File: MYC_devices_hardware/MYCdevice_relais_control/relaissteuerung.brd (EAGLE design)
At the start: 106.7 x 72.1 mm, 54 parts, among them IC1 MEGA8-P, IC2 7805T, K1 RT424012, K2 RT424012, K3 RT424012, K4 RT424012, Q1 20MHz, T1 BC547, T2 BC547, T3 BC547, T4 BC547

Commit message: adation to "0" based, and minor changes
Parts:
- removed C8: 18pF, resistor:C050-025X075
- removed C9: 100nF, resistor:C050-025X075
- removed R10: 3.3k, eagle-ltspice:0204/7
- added JP2: ISP, jumper:JP3Q
- added R12: 3.3k, rcl:0204V
- added X4, X5: 1503_09, con-lumberg:1503_09
- C1: value 100nF -> 22u 1206; device resistor:C050-025X075 -> resistor:C1206
- C2, C3: value 47uF -> 22u 1206; device rcl:TT5D10 -> resistor:C1206
- C4: value 100nF -> 18pF
- C6: device resistor:C050-025X075 -> resistor:C1206
- D1, D2, D3, D4, D5: device diode:DO41-10 -> zetex:E2LINE
- IC2: value 7805T -> 7805TV; device linear:TO220H -> linear:TO220V
- R1, R2, R4, R6: device rcl:0204/7 -> rcl:0204V
- R8: device eagle-ltspice:0204/7 -> rcl:0204V
- moved C3 57.1 mm to (87.6, 62.2), flipped to the bottom, turned to 0 degrees
- moved IC2 54.6 mm to (72.4, 43.2), turned to 0 degrees
- moved C4 52.4 mm to (97.8, 49.5), turned to 0 degrees
- moved R4 40.7 mm to (25.4, 36.8)
- moved R2 21.6 mm to (74.9, 53.3)
- moved R8 20.3 mm to (53.3, 38.1), turned to 270 degrees
- moved C2 19.9 mm to (76.2, 36.8), flipped to the bottom, turned to 0 degrees
- moved D5 18.0 mm to (73.7, 45.7), turned to 270 degrees
- moved R1 15.3 mm to (74.9, 49.5)
- moved C6 13.7 mm to (95.2, 62.2), flipped to the bottom
- moved SL1 11.7 mm to (85.1, 52.1), turned to 180 degrees
- moved C7 9.67 mm to (108.0, 52.1), turned to 90 degrees
- moved C1 9.25 mm to (69.8, 36.8), flipped to the bottom, turned to 180 degrees
- moved R6 8.98 mm to (40.6, 36.8), turned to 180 degrees
- moved JP1 8.13 mm to (108.0, 44.5)
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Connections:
- net N$37 renamed C5
- removed net N$1: IC1.27, R2.2, SL1.5
- new net N$37: IC1.27, R2.2, SL1.5, X4.3, X5.3
- new net N$56: C16.2, IC1.19, JP2.3, X1.A5
- net GND: now also C2.2, C3.1, C4.1, JP2.6, X4.1, X5.1; no longer C2.-, C3.-, C4.2, C8.1, C9.1
- net N$13: now also R8.2; no longer R6.1
- net N$15: now also R12.1; no longer R4.1
- net N$19: now also C4.2; no longer C8.2
- net N$22: now also R8.1; no longer R6.2
- net N$23: now also JP2.4
- net N$25: now also D5.2; no longer D5.A
- net N$26: now also R6.1; no longer R8.1
- net N$3: now also D1.1, D2.1, D3.1, D4.1, D5.1; no longer C2.+, D1.C, D2.C, D3.C, D4.C, D5.C
- net N$33: now also JP2.1
- net N$34: now also R6.2; no longer R8.2
- net N$35: now also C3.2; no longer C9.2
- net N$36: now also R12.2; no longer R4.2
- net N$40: now also D3.2; no longer D3.A
- net N$41: now also D2.2; no longer D2.A
- net N$42: now also D1.2; no longer D1.A
- net N$5: now also X4.2, X5.2
- net N$66: now also D4.2; no longer D4.A
- net N$67: now also R4.2; no longer R10.2
- net N$69: now also R4.1; no longer R10.1
- net N$7: now also IC1.1, JP2.5; no longer C16.2, IC1.19, X1.A5
- net VDD: now also C2.1, JP2.2; no longer C3.+, C4.1
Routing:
- net N$3: track 193.9 -> 108.2 mm
- net N$56: track 0.00 -> 46.2 mm
- net N$1: track 45.7 -> 0.00 mm
- net N$37: track 0.00 -> 39.6 mm
- net VDD: track 101.2 -> 77.8 mm
- net GND: track 238.4 -> 216.1 mm
- net N$7: track 35.5 -> 13.8 mm
- net N$69: track 91.4 -> 71.2 mm
- net N$26: track 69.8 -> 52.9 mm
- net N$5: track 40.6 -> 55.0 mm
- net N$55: track 48.2 -> 34.6 mm
- net N$23: track 35.5 -> 48.7 mm
- net N$33: track 35.5 -> 48.6 mm
- net N$22: track 48.3 -> 37.4 mm
- net N$62: track 45.7 -> 34.8 mm
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- added copper zone on layer 1, net GND
- added copper zone on layer 16, net GND
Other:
- board size 106.7 x 72.1 mm -> 106.7 x 59.7 mm
- board text added: "Relaissteuerung V02.0"
- board text removed: "Relaisteuerung V01.3"

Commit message: Modified Answer format
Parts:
- removed IC2: 7805TV, linear:TO220V
- added IC3: 78L05, v-reg:78LXX
- added JP3: Power, jumper:JP1
- R1, R2: device rcl:0204V -> resistor:R1206
- X1: value (none) -> Inputs
- X2: value (none) -> Relais1
- X3: value (none) -> Relais2
- moved R1 22.9 mm to (94.0, 36.8), flipped to the bottom, turned to 180 degrees
- moved R2 14.4 mm to (85.1, 43.2), flipped to the bottom, turned to 90 degrees
- moved D5 2.54 mm to (71.1, 45.7)
- moved C4 1.27 mm to (99.1, 49.5), turned to 180 degrees
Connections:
- new net N$58: C6.1, IC1.20, IC1.7, JP2.2, JP3.2
- net GND: now also IC3.GND; no longer IC2.2
- net N$3: now also IC3.IN; no longer IC2.1
- net VDD: now also IC3.OUT, JP3.1; no longer C6.1, IC1.20, IC1.7, IC2.3, JP2.2
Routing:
- net N$58: track 0.00 -> 70.6 mm
- net VDD: track 77.8 -> 30.1 mm
- net N$37: track 39.6 -> 53.0 mm
- net N$3: track 108.2 -> 118.5 mm
- net N$5: track 55.0 -> 61.9 mm
- net GND: track 216.1 -> 213.1 mm
- net N$25: track 18.1 -> 20.1 mm
- net N$19: track 10.6 -> 9.14 mm
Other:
- board text added: "1"
- board text added: "Relaissteuerung 2.1"
- board text removed: "Relaissteuerung V02.0"

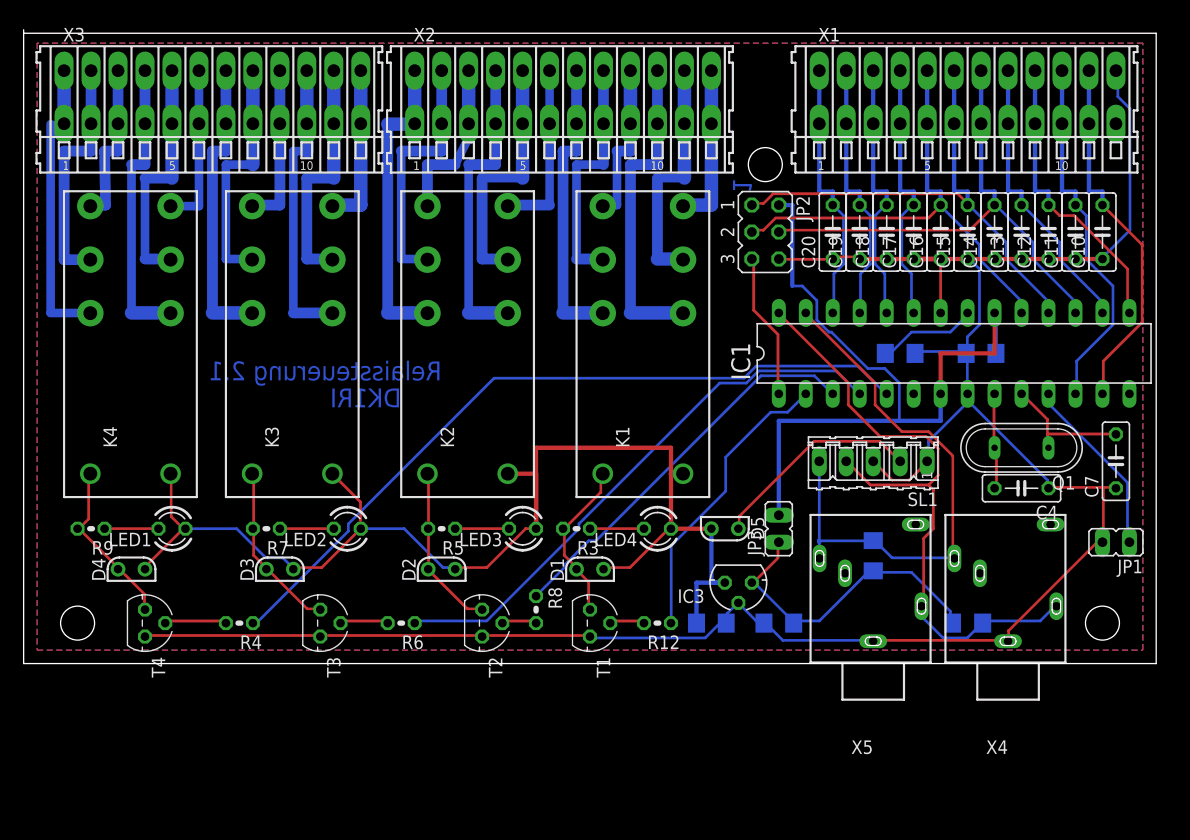
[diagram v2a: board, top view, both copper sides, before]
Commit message: new connector, I2C with 3V
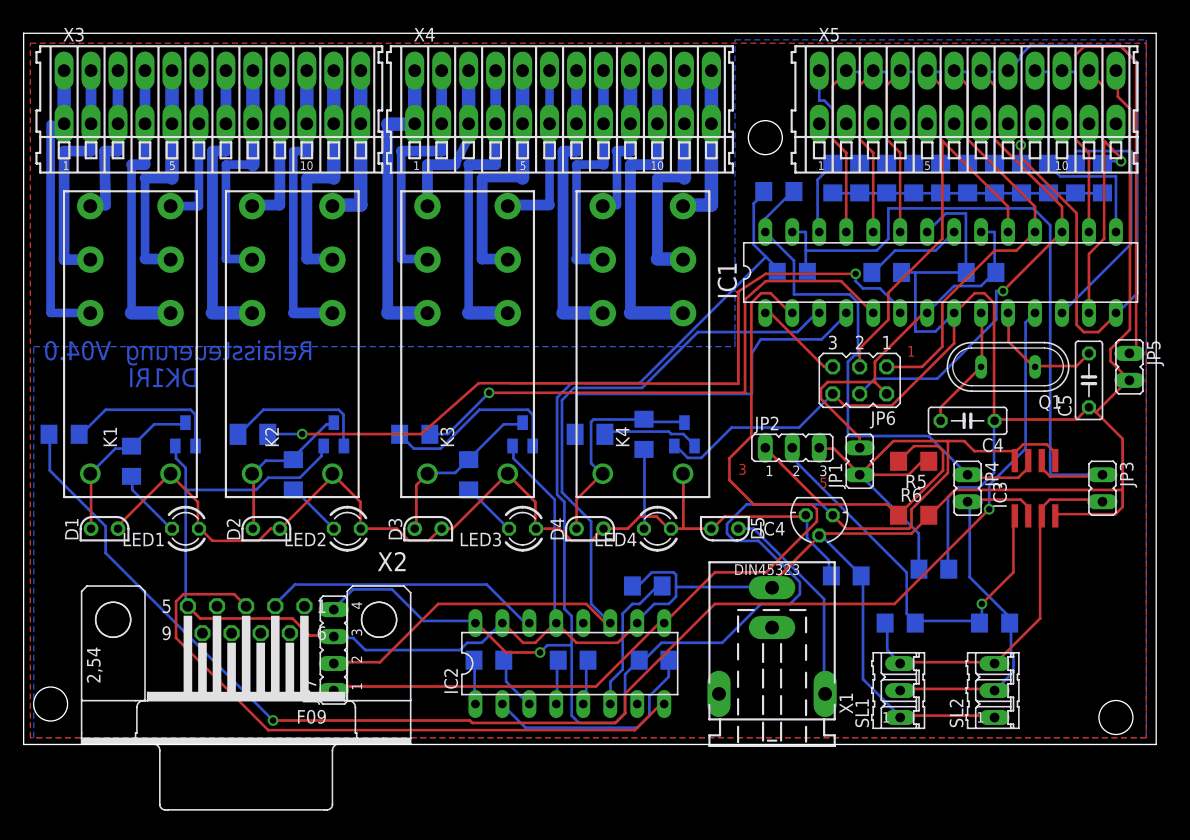
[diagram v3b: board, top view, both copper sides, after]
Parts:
- added C21: 22u, resistor:C1206
- added C5: 18pF, resistor:C050-025X075
- added C8, C9: 22uF, rcl:C1206
- added IC2: MAX232, maxim:DIL16
- added IC4: 78L05, v-reg:78LXX
- added JP4: SCL, jumper:JP1
- added JP5: Reset, jumper:JP1
- added JP6: ISP, jumper:JP3Q
- added JP7: USB, jumper:JP4
- added R10, R14: 3.3k, rcl:R1206
- added R11: 10k, rcl:R1206
- added R13: 10k, rcl:M1206
- added SL2: I2C, con-amp-quick:03P
- C1, C2, C3: value 22u 1206 -> 22uF
- C10, C11, C12, C13, C14, C15, C16, C17, C18, C19, C20: device resistor:C050-025X075 -> resistor:C1206
- C6: value 100nF -> 22uF; device resistor:C1206 -> rcl:C1206
- C7: value 18pF -> 22uF; device resistor:C050-025X075 -> rcl:C1206
- IC3: value 78L05 -> PCA9517; device v-reg:78LXX -> PCA9517:SO-08
- JP1: value Reset -> Power
- JP2: value ISP -> 3V/5V; device jumper:JP3Q -> jumper:JP2
- JP3: value Power -> SDA
- LED1: value (none) -> 1
- R1, R2: value 4k7 -> see manual
- R12, R8: device rcl:0204V -> rcl:R1206
- R3, R4: value 3.3k -> see manual; device rcl:0204V -> resistor:R1206
- R5: value 3.3k -> 1k; device rcl:0204V -> resistor:R1206
- R6: value 3.3k -> 1k5; device rcl:0204V -> resistor:R1206
- R7: value 3.3k -> 10k; device rcl:0204V -> rcl:R1206
- R9: value 3.3k -> 10k; device rcl:0204V -> rcl:M1206
- SL1: value I2C/Power -> I2C; device con-amp-quick:05P -> con-amp-quick:03P
- T1, T2, T3, T4: value BC547 -> (none); device transistor:TO92 -> transistor-neu-to92:SOT23-BEC
- X1: value Inputs -> Power; device con-wago255:233-512 -> con-conrad:737992-5
- X2: value Relais1 -> RS232; device con-wago255:233-512 -> con-subd:F09H
- X4: value 1503_09 -> Relais1; device con-lumberg:1503_09 -> con-wago255:233-512
- X5: value 1503_09 -> Inputs; device con-lumberg:1503_09 -> con-wago255:233-512
- moved X4 67.8 mm to (55.9, 86.4), turned to 0 degrees
- moved R4 65.1 mm to (76.2, 77.5), flipped to the bottom
- moved X1 59.1 mm to (75.6, 30.2)
- moved X2 57.6 mm to (26.0, 37.1), turned to 180 degrees
- moved C6 54.6 mm to (48.9, 33.3)
- moved C7 54.4 mm to (56.8, 33.3), flipped to the bottom, turned to 0 degrees
- moved X5 54.1 mm to (94.0, 86.4), turned to 0 degrees
- moved T4 53.8 mm to (67.3, 54.6), flipped to the bottom, turned to 0 degrees
- moved R6 49.3 mm to (88.9, 47.0), turned to 0 degrees
- moved K1 48.3 mm to (15.2, 63.5)
- moved K4 48.3 mm to (63.5, 63.5)
- moved D1 45.9 mm to (12.7, 45.7)
- moved R5 44.9 mm to (88.9, 52.1)
- moved D4 43.3 mm to (58.4, 45.7)
- moved T1 42.0 mm to (20.3, 54.6), flipped to the bottom, turned to 0 degrees
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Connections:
- new net N$57: IC3.3, JP3.2, R1.2, SL1.3, SL2.3
- new net N$59: IC3.1, JP2.2, R1.1, R2.1
- new net N$60: IC2.14, X2.2
- new net N$63: JP2.1, R5.2, R6.1
- new net N$64: IC2.8, X2.3
- new net N$70: C9.2, IC2.6
- new net N$71: C8.1, IC2.2
- new net N$72: C7.1, IC2.5
- new net N$73: C7.2, IC2.4
- new net N$74: C6.1, IC2.3
- new net N$75: C6.2, IC2.1
- new net RXD: IC1.2, IC2.9, JP7.1
- new net SCL: IC1.28, IC3.7, JP4.1, R4.2
- new net SDA: IC1.27, IC3.6, JP3.1, R3.2
- new net TXD: IC1.3, IC2.11, JP7.2
- net C5: now also C5.2; no longer C7.2
- net GND: now also C21.2, C5.1, C9.1, IC2.10, IC2.13, IC2.15, IC3.4, IC4.GND, JP5.2, JP6.6, JP7.3, R6.2, SL2.1, T1.E, T2.E, T3.E, T4.E, X1.+, X2.5, X5.A12; no longer C10.1, C11.1, C12.1, C13.1, C14.1, C15.1, C16.1, C17.1, C18.1, C19.1, C20.1, C6.2, C7.1, IC3.GND, JP1.2, JP2.6, SL1.3, T1.1, T2.1, T3.1, T4.1, X1.A12, X4.1, X5.1
- net N$10: now also K4.24, X4.A9; no longer K1.24, X2.A9
- net N$11: now also K4.21, X4.A8; no longer K1.21, X2.A8
- net N$12: now also K4.22, X4.A7; no longer K1.22, X2.A7
- net N$13: now also R11.2, T3.B; no longer R8.2, T2.2
- net N$15: now also IC1.11, R7.1; no longer IC1.2, R12.1
- net N$16: now also K3.14, X4.A6; no longer K2.14, X2.A6
- net N$17: now also K3.11, X4.A5; no longer K2.11, X2.A5
- net N$18: now also K3.12, X4.A4; no longer K2.12, X2.A4
- net N$2: now also K4.14, X4.A12; no longer K1.14, X2.A12
- net N$20: now also X5.A3; no longer X1.A3
- net N$21: now also IC1.16, JP5.1; no longer IC1.11, JP1.1
- net N$22: now also IC1.6, R9.1; no longer IC1.3, R8.1
- net N$23: now also JP6.4, X5.A7; no longer JP2.4, X1.A7
- net N$24: now also IC1.14, X5.A8; no longer IC1.16, X1.A8
- net N$25: now also X1.-1; no longer SL1.2
- net N$26: now also R13.1; no longer R6.1
- net N$27: now also K3.24, X4.A3; no longer K2.24, X2.A3
- net N$28: now also K3.21, X4.A2; no longer K2.21, X2.A2
- net N$29: now also R14.1; no longer R3.1
- net N$3: now also IC4.IN; no longer IC3.IN
- net N$30: now also R12.1; no longer R5.1
- net N$31: now also X5.A9; no longer X1.A9
- net N$32: now also R10.1; no longer R7.1
- net N$33: now also JP6.1, X5.A6; no longer JP2.1, X1.A6
- net N$34: now also R9.2, T2.B; no longer R6.2, T3.2
- net N$36: now also R13.2, T4.B; no longer R12.2, T1.2
- net N$37: now also IC3.2, JP4.2, SL1.2, SL2.2; no longer IC1.27, SL1.5, X4.3, X5.3
- net N$38: now also X5.A2; no longer X1.A2
- net N$39: now also K3.22, X4.A1; no longer K2.22, X2.A1
- net N$4: now also X5.A1; no longer X1.A1
- net N$40: now also D2.2, K2.A2, R10.2, T2.C; no longer D3.2, K3.A2, R7.2, T3.3
- net N$41: now also D3.2, K3.A2, R12.2, T3.C; no longer D2.2, K2.A2, R5.2, T2.3
- net N$42: now also D4.2, K4.A2, R14.2, T4.C; no longer D1.2, K1.A2, R3.2, T1.3
- net N$43: now also K2.14; no longer K3.14
- net N$44: now also K2.11; no longer K3.11
- net N$45: now also K2.12; no longer K3.12
- net N$46: now also K2.21; no longer K3.21
- net N$47: now also K2.24; no longer K3.24
- net N$48: now also K2.22; no longer K3.22
- net N$49: now also K1.14; no longer K4.14
- net N$5: now also C10.1, C11.1, C12.1, C13.1, C14.1, C15.1, C16.1, C17.1, C18.1, C19.1, C20.1; no longer IC1.28, R1.2, SL1.4, X4.2, X5.2
- net N$50: now also K1.11; no longer K4.11
- net N$51: now also K1.12; no longer K4.12
- net N$52: now also K1.24; no longer K4.24
- net N$53: now also K1.21; no longer K4.21
- net N$54: now also K1.22; no longer K4.22
- net N$55: now also X5.A10; no longer X1.A10
- net N$56: now also JP6.3, X5.A5; no longer JP2.3, X1.A5
- net N$58: now also C21.1, JP1.2, JP6.2; no longer C6.1, JP2.2, JP3.2
- net N$6: now also K4.11, X4.A11; no longer K1.11, X2.A11
- net N$62: now also X5.A11; no longer X1.A11
- net N$65: now also R8.1; no longer R9.1
- net N$66: now also D1.2, K1.A2, R8.2, T1.C; no longer D4.2, K4.A2, R9.2, T4.3
- net N$67: now also R7.2, T1.B; no longer R4.2, T4.2
- net N$69: now also R11.1; no longer R4.1
- net N$7: now also JP6.5; no longer JP2.5
- net N$8: now also X5.A4; no longer X1.A4
- net N$9: now also K4.12, X4.A10; no longer K1.12, X2.A10
- net VDD: now also C8.2, IC2.16, IC3.5, IC3.8, IC4.OUT, JP1.1, JP2.3, JP7.4, R3.1, R4.1, R5.1; no longer IC3.OUT, JP3.1, R1.1, R2.1
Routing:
- net VDD: track 30.1 -> 205.3 mm, vias 0 -> 1
- net GND: track 213.1 -> 341.7 mm
- net N$15: track 27.8 -> 132.9 mm, vias 0 -> 2
- net RXD: track 0.00 -> 85.2 mm
- net TXD: track 0.00 -> 79.8 mm
- net SDA: track 0.00 -> 67.4 mm
- net N$64: track 0.00 -> 61.5 mm
- net SCL: track 0.00 -> 51.2 mm
- net N$59: track 0.00 -> 39.2 mm, vias 0 -> 1
- net N$24: track 27.3 -> 64.1 mm, vias 0 -> 1
- net N$57: track 0.00 -> 36.2 mm
- net N$5: track 61.9 -> 25.7 mm
- net N$21: track 17.1 -> 52.8 mm
- net N$22: track 37.4 -> 72.9 mm, vias 0 -> 2
- net N$58: track 70.6 -> 35.9 mm
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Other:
- board size 106.7 x 59.7 mm -> 106.7 x 67 mm
- board text added: "3"
- board text added: "5"
- board text added: "Relaissteuerung"
- board text added: "V04.0"
- board text removed: "Relaissteuerung 2.1"
